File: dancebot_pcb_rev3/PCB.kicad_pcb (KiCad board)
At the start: 2 copper layers, 63.5 x 53.3 mm, 30 parts, among them J1 Voltage Regulator, J10 NeoPixel Right Eye, J11 Rocker Switch, J2 IO14 servo 1, J3 IO13 servo 2, J4 IO12 servo 3, J5 IO15 servo 4, J6 IO18 servo 5 (hat), J8 Pins, J9 NeoPixel Left Eye, Q1 IRLML6402TRPBF, U1 IRLML2502TRPBF, U2 ESP32-DEVKITC-32U

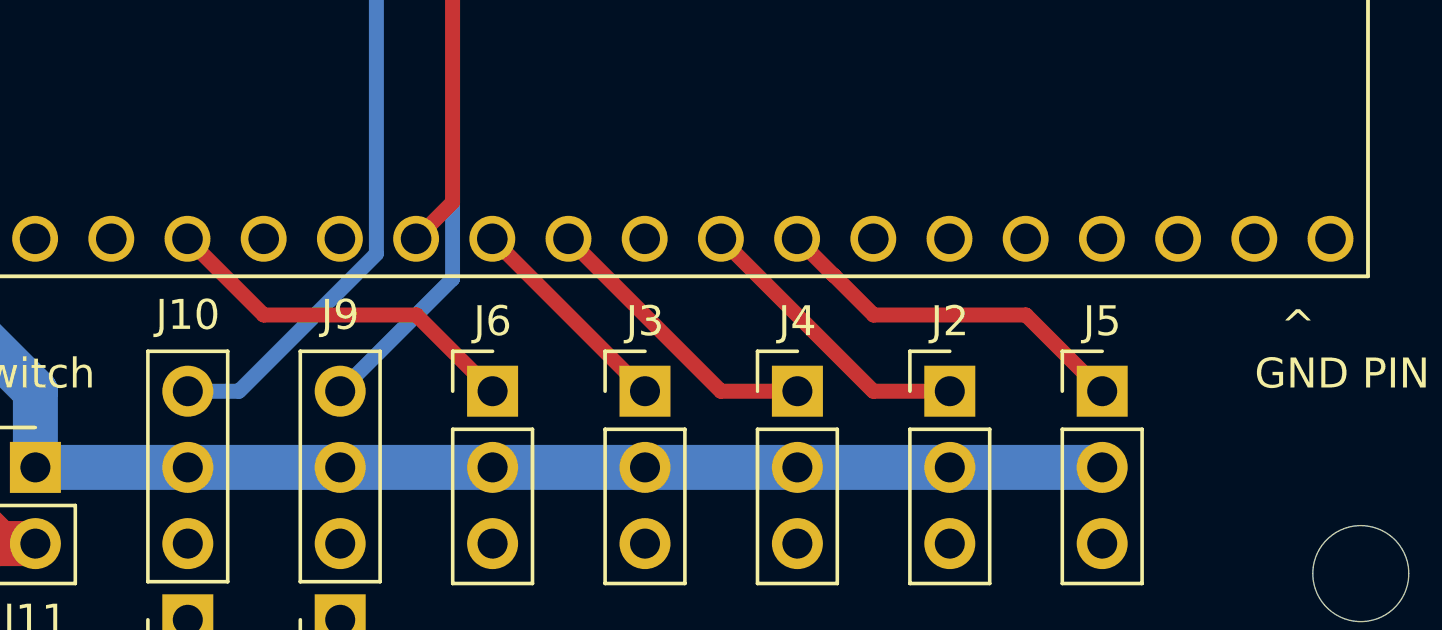
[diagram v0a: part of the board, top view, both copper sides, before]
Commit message: shifted servo control pins to not occupy gpio15, a pin used during bootup
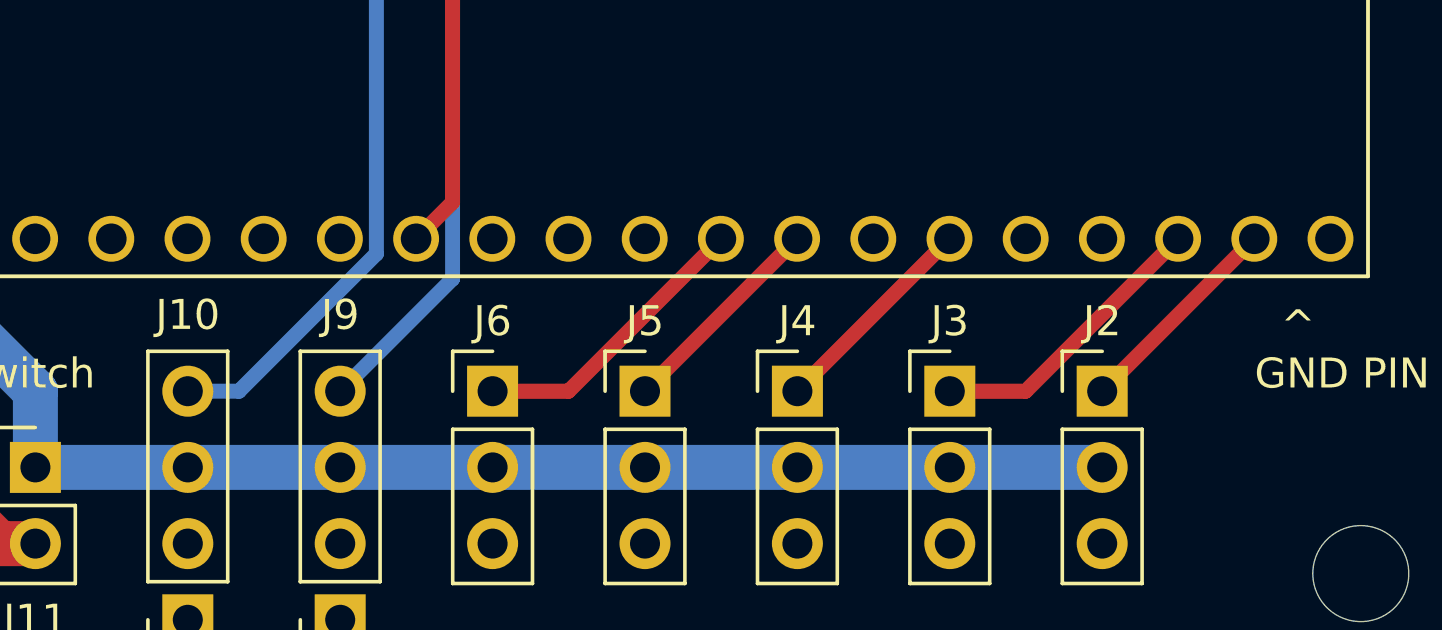
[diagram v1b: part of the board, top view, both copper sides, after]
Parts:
- moved J5 15.2 mm to (233.7, 116.8)
- moved J3 10.2 mm to (243.8, 116.8)
- moved J2 5.08 mm to (248.9, 116.8)
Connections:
- U2 pad 23: SM5 -> unconnected-(U2-IO15-Pad23)
- U2 pad 27: SM2 -> unconnected-(U2-IO16-Pad27)
- U2 pad 28: SM3 -> unconnected-(U2-IO17-Pad28)
- U2 pad 30: SM1 -> SM5
- U2 pad 33: unconnected-(U2-IO21-Pad33) -> SM3
- U2 pad 36: unconnected-(U2-IO22-Pad36) -> SM2
- U2 pad 37: unconnected-(U2-IO23-Pad37) -> SM1
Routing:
- net SM4: track 12.3 -> 7.19 mm
- net SM5: track 12.3 -> 9.71 mm
- net SM1: track 9.73 -> 7.18 mm
- net SM3: track 9.73 -> 7.18 mm
- net SM2: track 7.19 -> 9.71 mm
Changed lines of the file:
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@@
   (net 40 "unconnected-(U2-IO0-Pad25)")
   (net 41 "unconnected-(U2-IO5-Pad29)")
-  (net 42 "unconnected-(U2-IO21-Pad33)")
+  (net 42 "unconnected-(U2-IO15-Pad23)")
   (net 43 "unconnected-(U2-RXD0-Pad34)")
   (net 44 "unconnected-(U2-TXD0-Pad35)")
-  (net 45 "unconnected-(U2-IO22-Pad36)")
-  (net 46 "unconnected-(U2-IO23-Pad37)")
+  (net 45 "unconnected-(U2-IO16-Pad27)")
+  (net 46 "unconnected-(U2-IO17-Pad28)")
   (footprint "TestPoint:TestPoint_Pad_2.0x2.0mm" (layer "F.Cu")
     (at 233.68 81.28)
@@
   )
   (footprint "Connector_PinHeader_2.54mm:PinHeader_1x03_P2.54mm_Vertical" (layer "F.Cu")
-    (at 233.68 116.84)
+    (at 243.84 116.84)
     (descr "Through hole straight pin header, 1x03, 2.54mm pitch, single row")
     (tags "Through hole pin header THT 1x03 2.54mm single row")
@@
   )
   (footprint "Connector_PinHeader_2.54mm:PinHeader_1x03_P2.54mm_Vertical" (layer "F.Cu")
-    (at 248.92 116.84)
+    (at 233.68 116.84)
     (descr "Through hole straight pin header, 1x03, 2.54mm pitch, single row")
     (tags "Through hole pin header THT 1x03 2.54mm single row")
@@
       (net 38 "unconnected-(U2-SD1-Pad22)") (pinfunction "SD1") (pintype "bidirectional+no_connect") (solder_mask_margin 0.102))
     (pad "23" thru_hole circle (at 12.7 15.25 270) (size 1.53 1.53) (drill 1.02) (layers "*.Cu" "*.Mask")
-      (net 9 "SM5") (pinfunction "IO15") (pintype "bidirectional") (solder_mask_margin 0.102))
+      (net 42 "unconnected-(U2-IO15-Pad23)") (pinfunction "IO15") (pintype "bidirectional+no_connect") (solder_mask_margin 0.102))
     (pad "24" thru_hole circle (at 12.7 12.71 270) (size 1.53 1.53) (drill 1.02) (layers "*.Cu" "*.Mask")
       (net 39 "unconnected-(U2-IO2-Pad24)") (pinfunction "IO2") (pintype "bidirectional+no_connect") (solder_mask_margin 0.102))
@@
       (net 10 "BATT EN") (pinfunction "IO4") (pintype "bidirectional") (solder_mask_margin 0.102))
     (pad "27" thru_hole circle (at 12.7 5.09 270) (size 1.53 1.53) (drill 1.02) (layers "*.Cu" "*.Mask")
-      (net 6 "SM2") (pinfunction "IO16") (pintype "bidirectional") (solder_mask_margin 0.102))
+      (net 45 "unconnected-(U2-IO16-Pad27)") (pinfunction "IO16") (pintype "bidirectional+no_connect") (solder_mask_margin 0.102))
     (pad "28" thru_hole circle (at 12.7 2.55 270) (size 1.53 1.53) (drill 1.02) (layers "*.Cu" "*.Mask")
-      (net 7 "SM3") (pinfunction "IO17") (pintype "bidirectional") (solder_mask_margin 0.102))
+      (net 46 "unconnected-(U2-IO17-Pad28)") (pinfunction "IO17") (pintype "bidirectional+no_connect") (solder_mask_margin 0.102))
     (pad "29" thru_hole circle (at 12.7 0.01 270) (size 1.53 1.53) (drill 1.02) (layers "*.Cu" "*.Mask")
       (net 41 "unconnected-(U2-IO5-Pad29)") (pinfunction "IO5") (pintype "bidirectional+no_connect") (solder_mask_margin 0.102))
     (pad "30" thru_hole circle (at 12.7 -2.53 270) (size 1.53 1.53) (drill 1.02) (layers "*.Cu" "*.Mask")
-      (net 3 "SM1") (pinfunction "IO18") (pintype "bidirectional") (solder_mask_margin 0.102))
+      (net 9 "SM5") (pinfunction "IO18") (pintype "bidirectional") (solder_mask_margin 0.102))
     (pad "31" thru_hole circle (at 12.7 -5.07 270) (size 1.53 1.53) (drill 1.02) (layers "*.Cu" "*.Mask")
       (net 8 "SM4") (pinfunction "IO19") (pintype "bidirectional") (solder_mask_margin 0.102))
@@
       (net 1 "GND") (pinfunction "GND2") (pintype "power_in") (solder_mask_margin 0.102))
     (pad "33" thru_hole circle (at 12.7 -10.15 270) (size 1.53 1.53) (drill 1.02) (layers "*.Cu" "*.Mask")
-      (net 42 "unconnected-(U2-IO21-Pad33)") (pinfunction "IO21") (pintype "bidirectional+no_connect") (solder_mask_margin 0.102))
+      (net 7 "SM3") (pinfunction "IO21") (pintype "bidirectional") (solder_mask_margin 0.102))
     (pad "34" thru_hole circle (at 12.7 -12.69 270) (size 1.53 1.53) (drill 1.02) (layers "*.Cu" "*.Mask")
       (net 43 "unconnected-(U2-RXD0-Pad34)") (pinfunction "RXD0") (pintype "input+no_connect") (solder_mask_margin 0.102))
@@
       (net 44 "unconnected-(U2-TXD0-Pad35)") (pinfunction "TXD0") (pintype "output+no_connect") (solder_mask_margin 0.102))
     (pad "36" thru_hole circle (at 12.7 -17.77 270) (size 1.53 1.53) (drill 1.02) (layers "*.Cu" "*.Mask")
-      (net 45 "unconnected-(U2-IO22-Pad36)") (pinfunction "IO22") (pintype "bidirectional+no_connect") (solder_mask_margin 0.102))
+      (net 6 "SM2") (pinfunction "IO22") (pintype "bidirectional") (solder_mask_margin 0.102))
     (pad "37" thru_hole circle (at 12.7 -20.31 270) (size 1.53 1.53) (drill 1.02) (layers "*.Cu" "*.Mask")
-      (net 46 "unconnected-(U2-IO23-Pad37)") (pinfunction "IO23") (pintype "bidirectional+no_connect") (solder_mask_margin 0.102))
+      (net 3 "SM1") (pinfunction "IO23") (pintype "bidirectional") (solder_mask_margin 0.102))
     (pad "38" thru_hole circle (at 12.7 -22.85 270) (size 1.53 1.53) (drill 1.02) (layers "*.Cu" "*.Mask")
       (net 1 "GND") (pinfunction "GND3") (pintype "power_in") (solder_mask_margin 0.102))
@@
   )
   (footprint "Connector_PinHeader_2.54mm:PinHeader_1x03_P2.54mm_Vertical" (layer "F.Cu")
-    (at 243.84 116.84)
+    (at 248.92 116.84)
     (descr "Through hole straight pin header, 1x03, 2.54mm pitch, single row")
     (tags "Through hole pin header THT 1x03 2.54mm single row")
@@
   (segment (start 239.12 78.74) (end 246.37 85.99) (width 0.5) (layer "F.Cu") (net 2))
   (segment (start 214.2725 75.2875) (end 213.36 76.2) (width 0.5) (layer "F.Cu") (net 2))
-  (segment (start 241.29 116.84) (end 243.84 116.84) (width 0.5) (layer "F.Cu") (net 3))
-  (segment (start 236.21 111.76) (end 241.29 116.84) (width 0.5) (layer "F.Cu") (net 3))
+  (segment (start 248.92 116.83) (end 253.99 111.76) (width 0.5) (layer "F.Cu") (net 3))
+  (segment (start 248.92 116.84) (end 248.92 116.83) (width 0.5) (layer "F.Cu") (net 3))
   (segment (start 233.68 81.28) (end 233.68 86.35) (width 0.5) (layer "F.Cu") (net 4))
   (segment (start 233.68 86.35) (end 233.67 86.36) (width 0.5) (layer "F.Cu") (net 4))
@@
   (segment (start 227.265 113.095) (end 223.52 116.84) (width 0.5) (layer "B.Cu") (net 5))
   (segment (start 227.265 113.095) (end 227.265 95.305) (width 0.5) (layer "B.Cu") (net 5))
-  (segment (start 233.67 116.84) (end 233.68 116.84) (width 0.5) (layer "F.Cu") (net 6))
-  (segment (start 228.59 111.76) (end 233.67 116.84) (width 0.5) (layer "F.Cu") (net 6))
-  (segment (start 231.13 111.76) (end 236.21 116.84) (width 0.5) (layer "F.Cu") (net 7))
-  (segment (start 236.21 116.84) (end 238.76 116.84) (width 0.5) (layer "F.Cu") (net 7))
-  (segment (start 246.38 114.3) (end 248.92 116.84) (width 0.5) (layer "F.Cu") (net 8))
-  (segment (start 241.3 114.3) (end 246.38 114.3) (width 0.5) (layer "F.Cu") (net 8))
-  (segment (start 238.75 111.76) (end 239.965 112.975) (width 0.5) (layer "F.Cu") (net 8))
-  (segment (start 239.975 112.975) (end 241.3 114.3) (width 0.5) (layer "F.Cu") (net 8))
-  (segment (start 239.965 112.975) (end 239.975 112.975) (width 0.5) (layer "F.Cu") (net 8))
-  (segment (start 218.43 111.76) (end 220.97 114.3) (width 0.5) (layer "F.Cu") (net 9))
-  (segment (start 226.06 114.3) (end 228.6 116.84) (width 0.5) (layer "F.Cu") (net 9))
-  (segment (start 220.97 114.3) (end 226.06 114.3) (width 0.5) (layer "F.Cu") (net 9))
+  (segment (start 246.37 116.84) (end 251.45 111.76) (width 0.5) (layer "F.Cu") (net 6))
+  (segment (start 243.84 116.84) (end 246.37 116.84) (width 0.5) (layer "F.Cu") (net 6))
+  (segment (start 238.76 116.83) (end 243.83 111.76) (width 0.5) (layer "F.Cu") (net 7))
+  (segment (start 238.76 116.84) (end 238.76 116.83) (width 0.5) (layer "F.Cu") (net 7))
+  (segment (start 233.67 116.84) (end 233.68 116.84) (width 0.5) (layer "F.Cu") (net 8))
+  (segment (start 233.68 116.84) (end 233.68 116.83) (width 0.5) (layer "F.Cu") (net 8))
+  (segment (start 233.68 116.83) (end 238.75 111.76) (width 0.5) (layer "F.Cu") (net 8))
+  (segment (start 228.6 116.84) (end 231.13 116.84) (width 0.5) (layer "F.Cu") (net 9))
+  (segment (start 231.13 116.84) (end 236.21 111.76) (width 0.5) (layer "F.Cu") (net 9))
   (segment (start 227.265 110.545) (end 227.265 83.3975) (width 0.5) (layer "F.Cu") (net 10))
   (segment (start 227.265 83.3975) (end 226.06 82.1925) (width 0.5) (layer "F.Cu") (net 10))

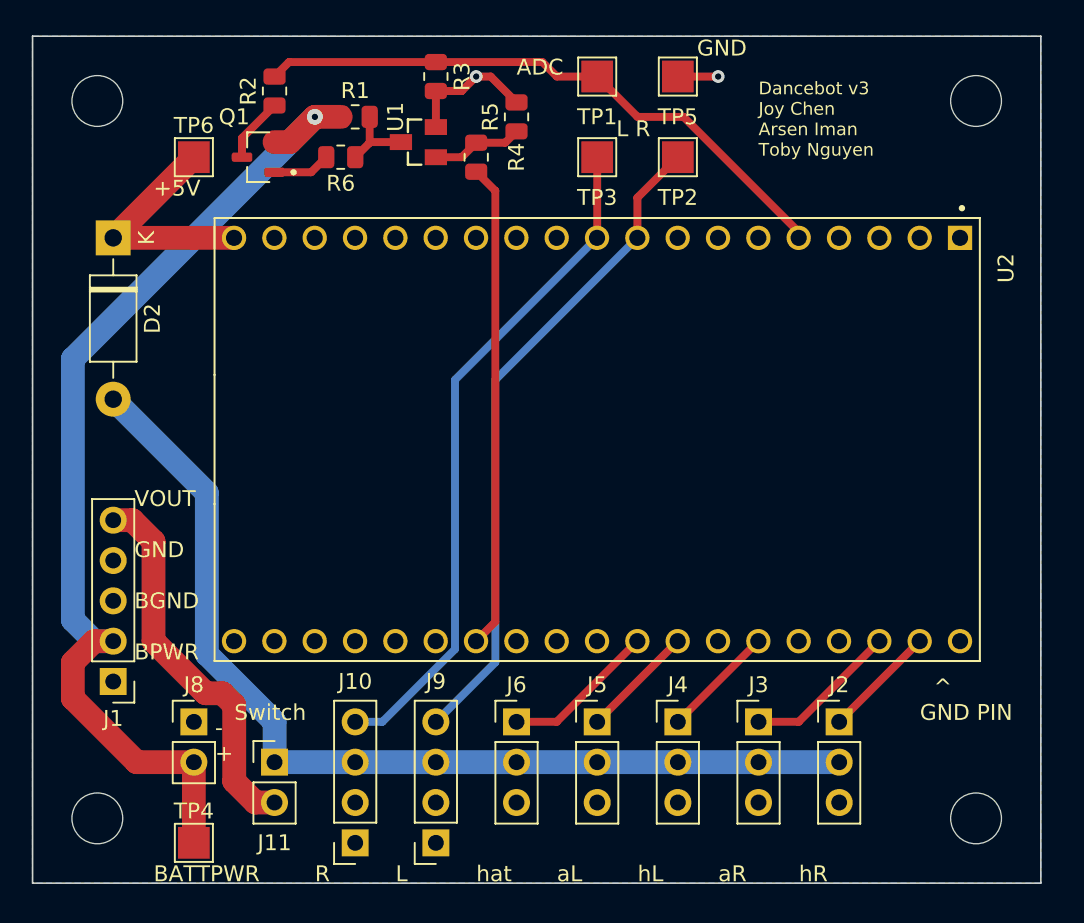
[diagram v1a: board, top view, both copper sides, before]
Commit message: fixed silkscreen
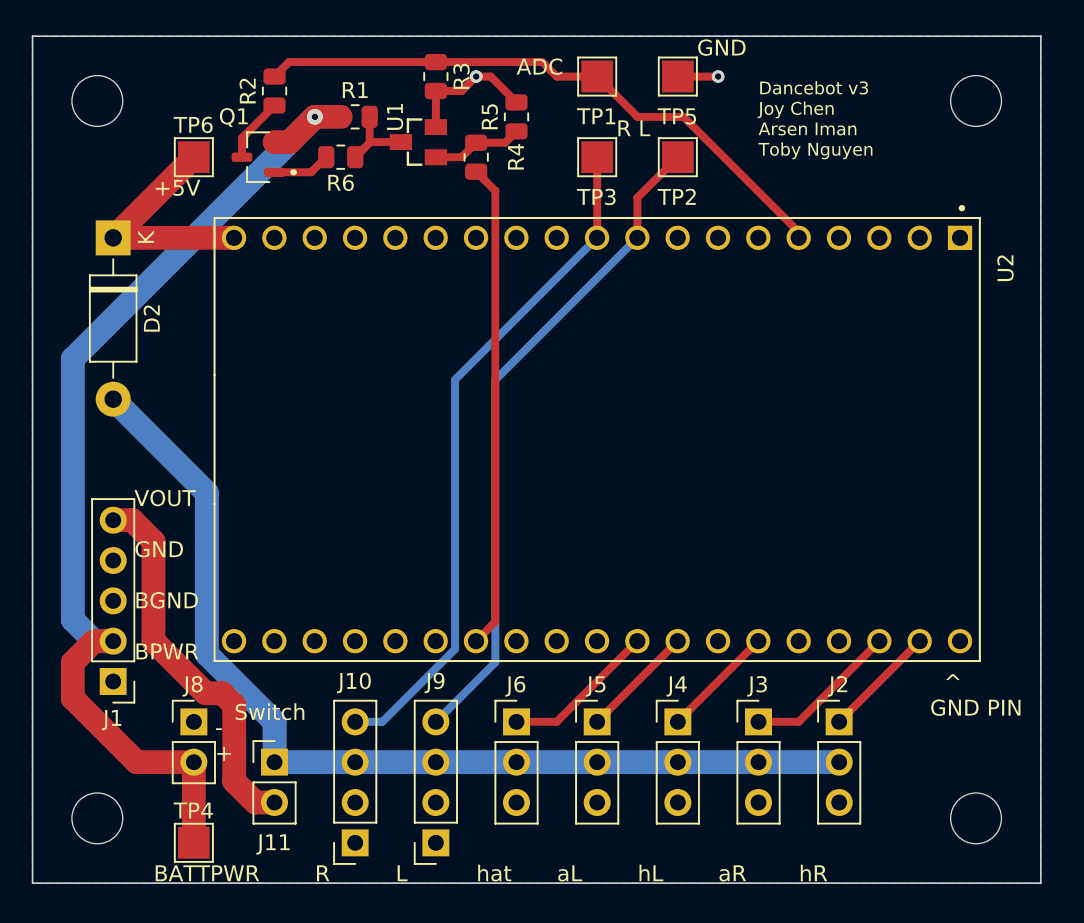
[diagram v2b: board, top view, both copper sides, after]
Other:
- board text added: "R L"
- board text removed: "L R"
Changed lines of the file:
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@@
     (effects (font (size 1 1) (thickness 0.15)) (justify left bottom))
   )
-  (gr_text "  ^\nGND PIN" (at 254 116.84) (layer "F.SilkS")
+  (gr_text "  ^\nGND PIN" (at 254.635692 116.569984) (layer "F.SilkS")
     (effects (font (size 1 1) (thickness 0.15)) (justify left bottom))
   )
@@
     (effects (font (size 1 1) (thickness 0.15)) (justify left bottom))
   )
-  (gr_text "L R" (at 234.88 80.08) (layer "F.SilkS")
+  (gr_text "R L" (at 234.88 80.08) (layer "F.SilkS")
     (effects (font (size 1 1) (thickness 0.15)) (justify left bottom))
   )
